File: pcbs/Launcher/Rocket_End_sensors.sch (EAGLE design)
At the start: 5 parts, among them U1 ARDUINO-MEGAPRO-5V, X1 22-23-2051, X3 22-23-2041

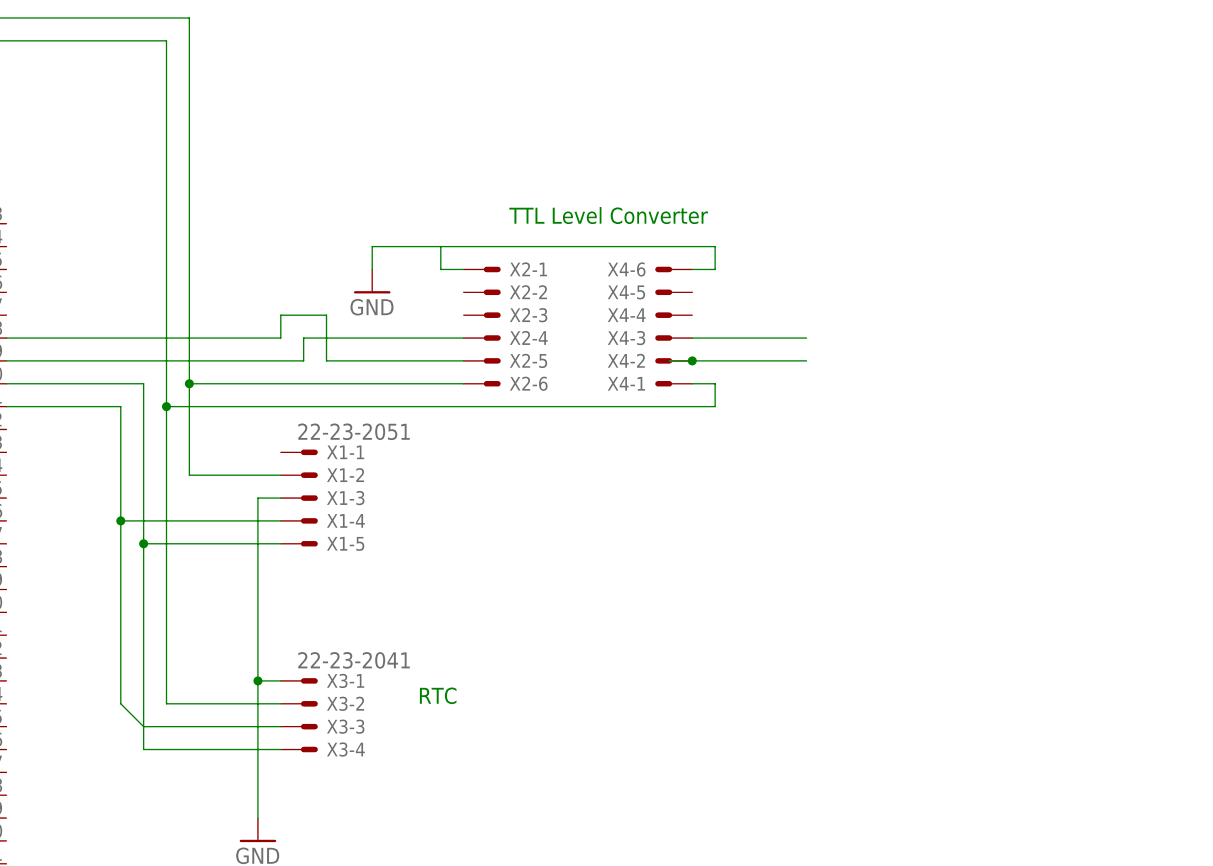
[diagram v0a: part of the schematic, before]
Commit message: * Adding GPS Module
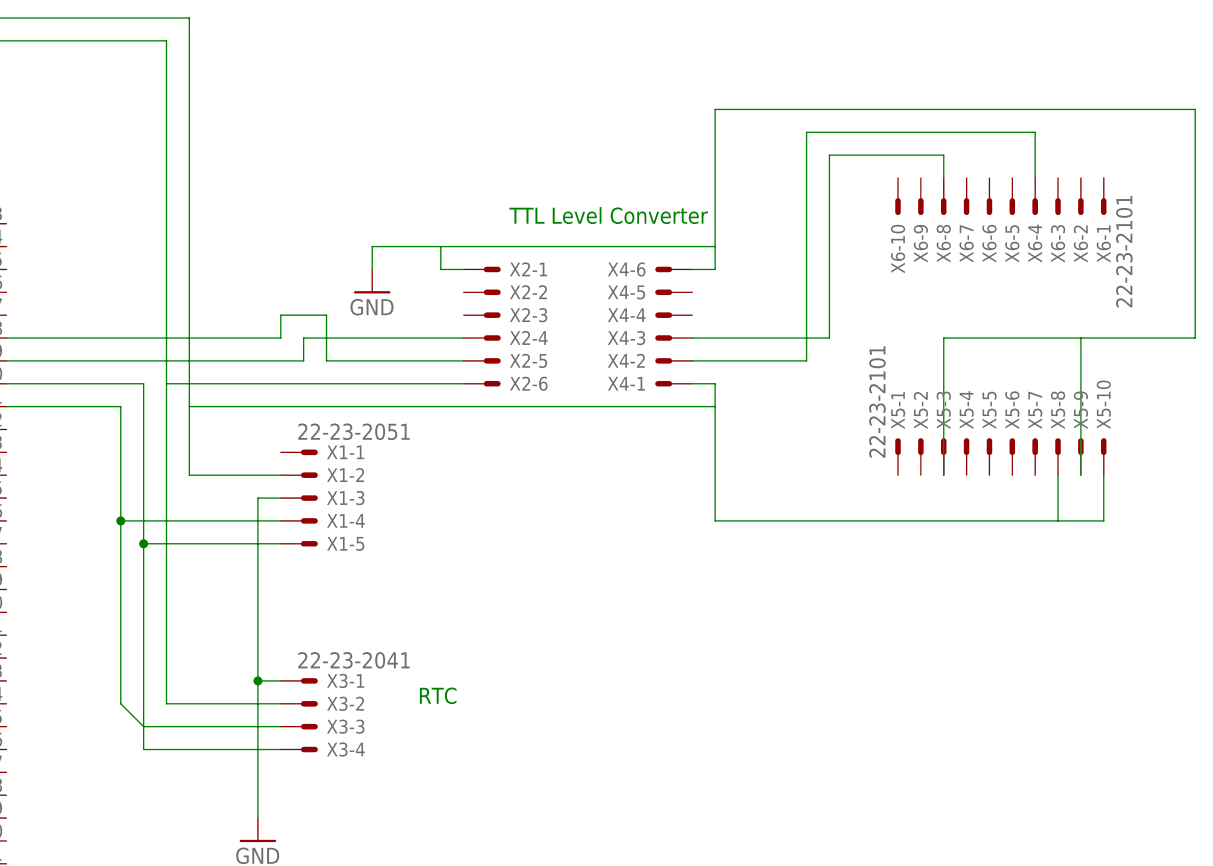
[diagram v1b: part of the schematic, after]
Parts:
- added X5, X6: 22-23-2101, con-molex:22-23-2101
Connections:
- removed net N$2: U1.3.3V, X1-2.S, X2-6.S
- removed net N$5: X4-3.S
- new net N$4: U1.3.3V, X1-2.S, X4-1.S, X5-10.S, X5-8.S
- new net N$8: X4-2.S, X6-4.S
- net GND: now also X5-3.S, X5-9.S
- net N$28: now also X2-6.S; no longer X4-1.S
- net N$6: now also X4-3.S, X6-8.S; no longer X4-2.S
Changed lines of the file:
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@@
 <part name="X4" library="con-molex" deviceset="22-23-2061" device=""/>
 <part name="GND2" library="supply1" deviceset="GND" device=""/>
+<part name="X5" library="con-molex" deviceset="22-23-2101" device=""/>
+<part name="X6" library="con-molex" deviceset="22-23-2101" device=""/>
 </parts>
 <sheets>
@@
 <instance part="X4" gate="-6" x="132.08" y="99.06" rot="R180"/>
 <instance part="GND2" gate="1" x="99.06" y="96.52"/>
+<instance part="X5" gate="-1" x="157.48" y="78.74" rot="R90"/>
+<instance part="X5" gate="-2" x="160.02" y="78.74" rot="R90"/>
+<instance part="X5" gate="-3" x="162.56" y="78.74" rot="R90"/>
+<instance part="X5" gate="-4" x="165.1" y="78.74" rot="R90"/>
+<instance part="X5" gate="-5" x="167.64" y="78.74" rot="R90"/>
+<instance part="X5" gate="-6" x="170.18" y="78.74" rot="R90"/>
+<instance part="X5" gate="-7" x="172.72" y="78.74" rot="R90"/>
+<instance part="X5" gate="-8" x="175.26" y="78.74" rot="R90"/>
+<instance part="X5" gate="-9" x="177.8" y="78.74" rot="R90"/>
+<instance part="X5" gate="-10" x="180.34" y="78.74" rot="R90"/>
+<instance part="X6" gate="-1" x="180.34" y="106.68" rot="R270"/>
+<instance part="X6" gate="-2" x="177.8" y="106.68" rot="R270"/>
+<instance part="X6" gate="-3" x="175.26" y="106.68" rot="R270"/>
+<instance part="X6" gate="-4" x="172.72" y="106.68" rot="R270"/>
+<instance part="X6" gate="-5" x="170.18" y="106.68" rot="R270"/>
+<instance part="X6" gate="-6" x="167.64" y="106.68" rot="R270"/>
+<instance part="X6" gate="-7" x="165.1" y="106.68" rot="R270"/>
+<instance part="X6" gate="-8" x="162.56" y="106.68" rot="R270"/>
+<instance part="X6" gate="-9" x="160.02" y="106.68" rot="R270"/>
+<instance part="X6" gate="-10" x="157.48" y="106.68" rot="R270"/>
 </instances>
 <busses>
@@
 <wire x1="99.06" y1="101.6" x2="99.06" y2="99.06" width="0.1524" layer="91"/>
 <pinref part="GND2" gate="1" pin="GND"/>
+<pinref part="X5" gate="-9" pin="S"/>
+<wire x1="177.8" y1="76.2" x2="177.8" y2="91.44" width="0.1524" layer="91"/>
+<wire x1="177.8" y1="91.44" x2="162.56" y2="91.44" width="0.1524" layer="91"/>
+<pinref part="X5" gate="-3" pin="S"/>
+<wire x1="162.56" y1="91.44" x2="162.56" y2="76.2" width="0.1524" layer="91"/>
+<wire x1="177.8" y1="91.44" x2="190.5" y2="91.44" width="0.1524" layer="91"/>
+<wire x1="190.5" y1="91.44" x2="190.5" y2="116.84" width="0.1524" layer="91"/>
+<wire x1="190.5" y1="116.84" x2="137.16" y2="116.84" width="0.1524" layer="91"/>
+<wire x1="137.16" y1="116.84" x2="137.16" y2="101.6" width="0.1524" layer="91"/>
 </segment>
 </net>
@@
 <net name="N$28" class="0">
 <segment>
-<wire x1="76.2" y1="50.8" x2="76.2" y2="83.82" width="0.1524" layer="91"/>
-<wire x1="76.2" y1="83.82" x2="76.2" y2="124.46" width="0.1524" layer="91"/>
+<wire x1="76.2" y1="50.8" x2="76.2" y2="86.36" width="0.1524" layer="91"/>
+<wire x1="76.2" y1="86.36" x2="76.2" y2="124.46" width="0.1524" layer="91"/>
 <wire x1="10.16" y1="99.06" x2="10.16" y2="124.46" width="0.1524" layer="91"/>
 <wire x1="10.16" y1="124.46" x2="76.2" y2="124.46" width="0.1524" layer="91"/>
@@
 <pinref part="X3" gate="-2" pin="S"/>
 <wire x1="88.9" y1="50.8" x2="76.2" y2="50.8" width="0.1524" layer="91"/>
-<wire x1="76.2" y1="83.82" x2="137.16" y2="83.82" width="0.1524" layer="91"/>
-<wire x1="137.16" y1="83.82" x2="137.16" y2="86.36" width="0.1524" layer="91"/>
-<pinref part="X4" gate="-1" pin="S"/>
-<wire x1="137.16" y1="86.36" x2="134.62" y2="86.36" width="0.1524" layer="91"/>
-<junction x="76.2" y="83.82"/>
-</segment>
-</net>
-<net name="N$2" class="0">
-<segment>
-<wire x1="7.62" y1="93.98" x2="7.62" y2="127" width="0.1524" layer="91"/>
-<wire x1="7.62" y1="127" x2="78.74" y2="127" width="0.1524" layer="91"/>
-<wire x1="78.74" y1="127" x2="78.74" y2="86.36" width="0.1524" layer="91"/>
-<pinref part="X1" gate="-2" pin="S"/>
-<wire x1="78.74" y1="86.36" x2="78.74" y2="76.2" width="0.1524" layer="91"/>
-<wire x1="78.74" y1="76.2" x2="88.9" y2="76.2" width="0.1524" layer="91"/>
-<pinref part="U1" gate="G$1" pin="3.3V"/>
-<wire x1="17.78" y1="93.98" x2="7.62" y2="93.98" width="0.1524" layer="91"/>
 <pinref part="X2" gate="-6" pin="S"/>
-<wire x1="78.74" y1="86.36" x2="109.22" y2="86.36" width="0.1524" layer="91"/>
-<junction x="78.74" y="86.36"/>
+<wire x1="109.22" y1="86.36" x2="76.2" y2="86.36" width="0.1524" layer="91"/>
 </segment>
 </net>
@@
 <pinref part="X2" gate="-4" pin="S"/>
 <wire x1="109.22" y1="91.44" x2="91.44" y2="91.44" width="0.1524" layer="91"/>
-</segment>
-</net>
-<net name="N$5" class="0">
-<segment>
-<pinref part="X4" gate="-3" pin="S"/>
-<wire x1="134.62" y1="91.44" x2="147.32" y2="91.44" width="0.1524" layer="91"/>
-</segment>
-</net>
-<net name="N$6" class="0">
-<segment>
-<wire x1="132.08" y1="88.9" x2="134.62" y2="88.9" width="0.1524" layer="91"/>
-<pinref part="X4" gate="-2" pin="S"/>
-<wire x1="134.62" y1="88.9" x2="147.32" y2="88.9" width="0.1524" layer="91"/>
-<junction x="134.62" y="88.9"/>
 </segment>
 </net>
@@
 </segment>
 </net>
+<net name="N$4" class="0">
+<segment>
+<pinref part="X5" gate="-10" pin="S"/>
+<wire x1="180.34" y1="76.2" x2="180.34" y2="71.12" width="0.1524" layer="91"/>
+<wire x1="180.34" y1="71.12" x2="175.26" y2="71.12" width="0.1524" layer="91"/>
+<pinref part="X5" gate="-8" pin="S"/>
+<wire x1="175.26" y1="71.12" x2="175.26" y2="76.2" width="0.1524" layer="91"/>
+<pinref part="X4" gate="-1" pin="S"/>
+<wire x1="137.16" y1="83.82" x2="137.16" y2="86.36" width="0.1524" layer="91"/>
+<wire x1="137.16" y1="86.36" x2="134.62" y2="86.36" width="0.1524" layer="91"/>
+<wire x1="7.62" y1="93.98" x2="7.62" y2="127" width="0.1524" layer="91"/>
+<wire x1="7.62" y1="127" x2="78.74" y2="127" width="0.1524" layer="91"/>
+<wire x1="78.74" y1="127" x2="78.74" y2="83.82" width="0.1524" layer="91"/>
+<pinref part="X1" gate="-2" pin="S"/>
+<wire x1="78.74" y1="83.82" x2="78.74" y2="76.2" width="0.1524" layer="91"/>
+<wire x1="78.74" y1="76.2" x2="88.9" y2="76.2" width="0.1524" layer="91"/>
+<pinref part="U1" gate="G$1" pin="3.3V"/>
+<wire x1="17.78" y1="93.98" x2="7.62" y2="93.98" width="0.1524" layer="91"/>
+<wire x1="137.16" y1="83.82" x2="78.74" y2="83.82" width="0.1524" layer="91"/>
+<wire x1="175.26" y1="71.12" x2="137.16" y2="71.12" width="0.1524" layer="91"/>
+<wire x1="137.16" y1="71.12" x2="137.16" y2="83.82" width="0.1524" layer="91"/>
+</segment>
+</net>
+<net name="N$8" class="0">
+<segment>
+<wire x1="147.32" y1="88.9" x2="147.32" y2="114.3" width="0.1524" layer="91"/>
+<pinref part="X6" gate="-4" pin="S"/>
+<wire x1="172.72" y1="109.22" x2="172.72" y2="114.3" width="0.1524" layer="91"/>
+<wire x1="172.72" y1="114.3" x2="147.32" y2="114.3" width="0.1524" layer="91"/>
+<pinref part="X4" gate="-2" pin="S"/>
+<wire x1="134.62" y1="88.9" x2="147.32" y2="88.9" width="0.1524" layer="91"/>
+</segment>
+</net>
+<net name="N$6" class="0">
+<segment>
+<wire x1="149.86" y1="91.44" x2="134.62" y2="91.44" width="0.1524" layer="91"/>
+<pinref part="X6" gate="-8" pin="S"/>
+<wire x1="162.56" y1="109.22" x2="162.56" y2="111.76" width="0.1524" layer="91"/>
+<wire x1="162.56" y1="111.76" x2="149.86" y2="111.76" width="0.1524" layer="91"/>
+<wire x1="149.86" y1="111.76" x2="149.86" y2="91.44" width="0.1524" layer="91"/>
+<pinref part="X4" gate="-3" pin="S"/>
+</segment>
+</net>
